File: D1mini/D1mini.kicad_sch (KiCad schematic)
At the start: 4 parts, among them U1 CH340C

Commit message: 20250807 modify
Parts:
- removed U1: CH340C, Package_SO:SOIC-16_3.9x9.9mm_P1.27mm, symbol Interface_USB:CH340C
- added D1, D2, D3, D4: LED_Filled, LED_THT:LED_D5.0mm_Clear, symbol Device:LED_Filled
- added H1, H2, H3, H4: MountingHole, MountingHole:MountingHole_3.2mm_M3_Pad_Via, symbol Mechanical:MountingHole
- added J1: USB_B, Connector_USB:USB_B_TE_5787834_Vertical, symbol Connector:USB_B
- added R2, R4: 10k, Resistor_THT:R_Axial_DIN0207_L6.3mm_D2.5mm_P7.62mm_Horizontal, symbol Device:R_US
- added R3: 1k, Resistor_THT:R_Axial_DIN0207_L6.3mm_D2.5mm_P7.62mm_Horizontal, symbol Device:R_US
- added R5: 10, Resistor_THT:R_Axial_DIN0207_L6.3mm_D2.5mm_P7.62mm_Horizontal, symbol Device:R_US
- added U1, U2: LM555xN, Package_DIP:DIP-8_W7.62mm, symbol Timer:LM555xN
- C1, C2: value C_US -> 100u; footprint (none) -> Capacitor_THT:CP_Axial_L10.0mm_D4.5mm_P15.00mm_Horizontal
- R1: value 470 -> 1k; footprint (none) -> Resistor_THT:R_Axial_DIN0207_L6.3mm_D2.5mm_P7.62mm_Horizontal
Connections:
- net GND: now also J1.4 (GND), J1.5 (Shield), U1.1 (GND), U2.1 (GND)
- net VCC: now reaches R1.1
- net VCC: now also J1.1 (VBUS), R3.1, U1.4 (R), U1.8 (VCC), U2.4 (R), U2.8 (VCC)
- net at R1.2: now also R2.1, U1.7 (DIS)
- net +3.3V: no longer names the net of C2.1
- net +3.3V: now also R4.2, U2.2 (TR), U2.6 (THR); no longer C1.1
- new net: D1.1 (K), D2.1 (K), D3.2 (A), D4.2 (A), R5.2
- new net: D1.2 (A), D2.2 (A), D3.1 (K), D4.1 (K), U2.3 (Q)
- new net: R3.2, R4.1, U2.7 (DIS)
- new net: R5.1, U1.3 (Q)
- new net: C1.1, R2.2, U1.2 (TR), U1.6 (THR)
- no-connect marks 5 -> 4

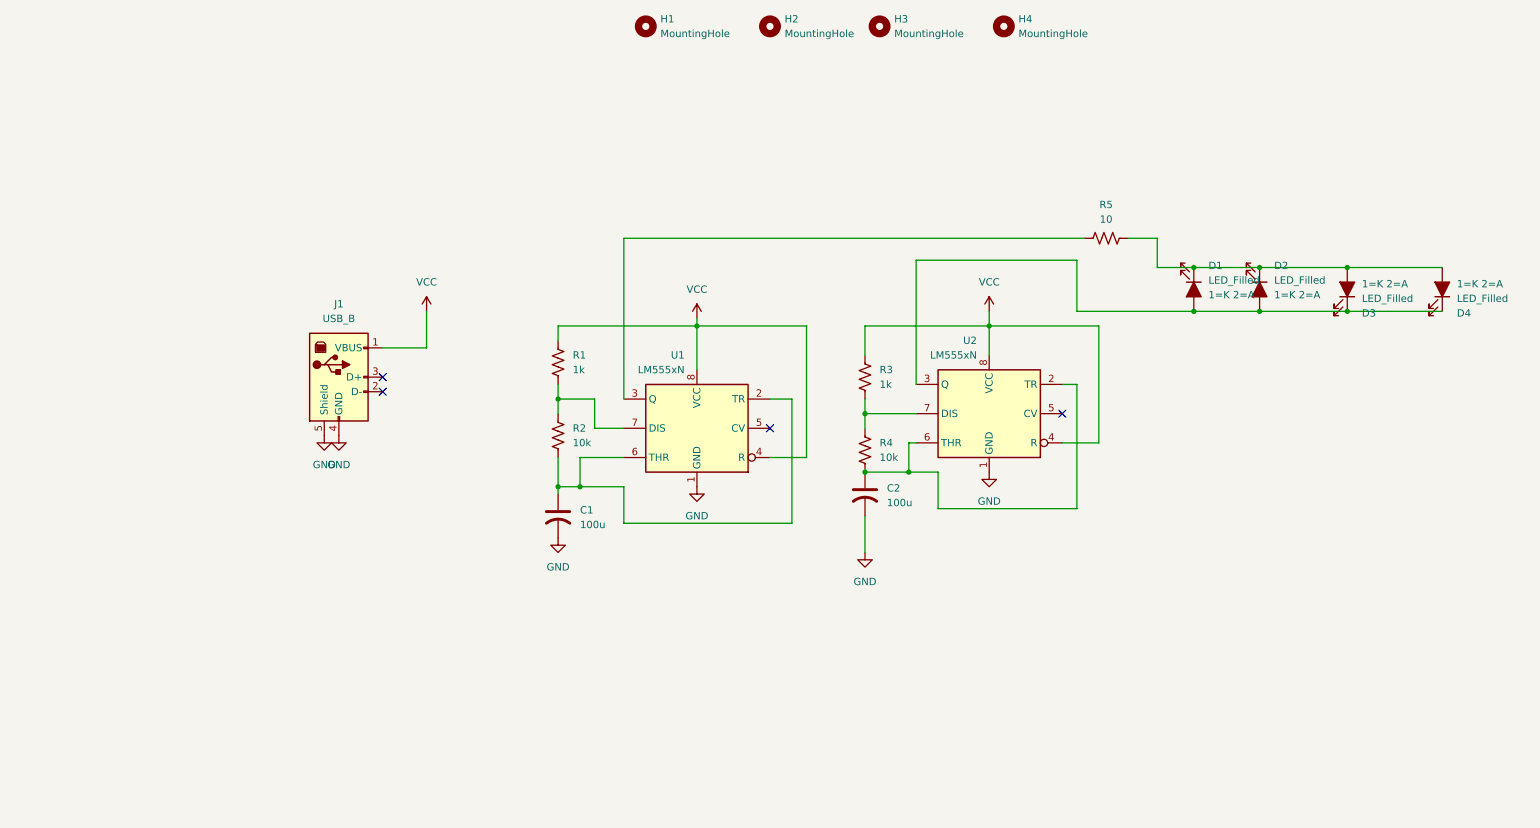
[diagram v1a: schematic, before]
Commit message: 新增新專案, usb to TTL
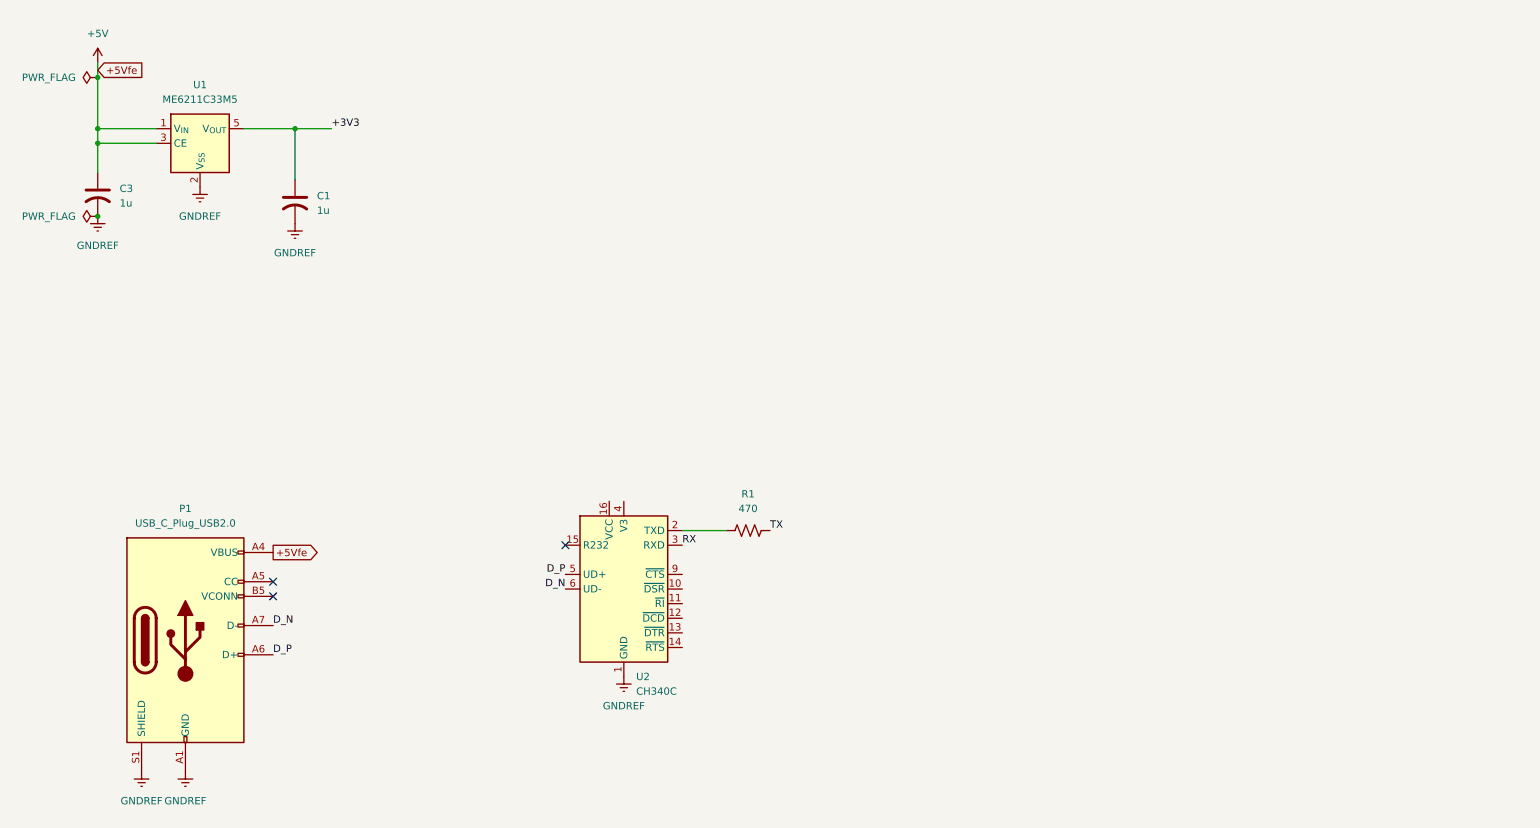
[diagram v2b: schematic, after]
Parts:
- removed C2: 100u, Capacitor_THT:CP_Axial_L10.0mm_D4.5mm_P15.00mm_Horizontal, symbol Device:C_US
- removed D1, D2, D3, D4: LED_Filled, LED_THT:LED_D5.0mm_Clear, symbol Device:LED_Filled
- removed H1, H2, H3, H4: MountingHole, MountingHole:MountingHole_3.2mm_M3_Pad_Via, symbol Mechanical:MountingHole
- removed J1: USB_B, Connector_USB:USB_B_TE_5787834_Vertical, symbol Connector:USB_B
- removed R2, R4: 10k, Resistor_THT:R_Axial_DIN0207_L6.3mm_D2.5mm_P7.62mm_Horizontal, symbol Device:R_US
- removed R3: 1k, Resistor_THT:R_Axial_DIN0207_L6.3mm_D2.5mm_P7.62mm_Horizontal, symbol Device:R_US
- removed R5: 10, Resistor_THT:R_Axial_DIN0207_L6.3mm_D2.5mm_P7.62mm_Horizontal, symbol Device:R_US
- removed U1, U2: LM555xN, Package_DIP:DIP-8_W7.62mm, symbol Timer:LM555xN
- added C3: 1u, Capacitor_SMD:C_0805_2012Metric_Pad1.18x1.45mm_HandSolder, symbol Device:C_US
- added P1: USB_C_Plug_USB2.0, Connector_USB:USB_C_Receptacle_GCT_USB4085, symbol Connector:USB_C_Plug_USB2.0
- added U1: ME6211C33M5, Package_TO_SOT_SMD:SOT-23-5, symbol Regulator_Linear:ME6211C33M5
- added U2: CH340C, Package_SO:SOIC-16_3.9x9.9mm_P1.27mm, symbol Interface_USB:CH340C
- C1: value 100u -> 1u; footprint Capacitor_THT:CP_Axial_L10.0mm_D4.5mm_P15.00mm_Horizontal -> Capacitor_SMD:C_0805_2012Metric_Pad1.18x1.45mm_HandSolder
- R1: value 1k -> 470; footprint Resistor_THT:R_Axial_DIN0207_L6.3mm_D2.5mm_P7.62mm_Horizontal -> Resistor_SMD:R_0805_2012Metric_Pad1.20x1.40mm_HandSolder
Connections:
- net TX: now reaches R1.2
- net +3V3: now reaches C1.1
- net +3V3: now also U1.5 (V_{OUT})
- net GND renamed GNDREF
- net GNDREF: now also C3.2, P1.A1 (GND), P1.A12 (GND), P1.B1 (GND), P1.B12 (GND), P1.S1 (SHIELD), U1.2 (V_{SS}), U2.1 (GND)
- net VCC: no longer names the net of R1.1
- net VCC: now also U2.2 (TXD)
- new net +5V: C3.1, P1.A4 (VBUS), P1.A9 (VBUS), P1.B4 (VBUS), P1.B9 (VBUS), U1.1 (V_{IN}), U1.3 (CE)
- new net D_N: P1.A7 (D-), U2.6 (UD-)
- new net D_P: P1.A6 (D+), U2.5 (UD+)
- new net RX: U2.3 (RXD)
- no-connect marks 4 -> 3
